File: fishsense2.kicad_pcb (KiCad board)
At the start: 2 copper layers, 86.4 x 49.5 mm, 39 parts, among them J1 Conn_02x10_Odd_Even, J11 Screw_Terminal_01x02, J2 BATT_OUT, J3 BATT_IN, K1 UMS05-1A80-75L, Q1 Q_NMOS_GSD, Q2 Q_NMOS_GSD, Q3 Q_NMOS_GSD, SW1 SW_Reed, SW2 SW_Reed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

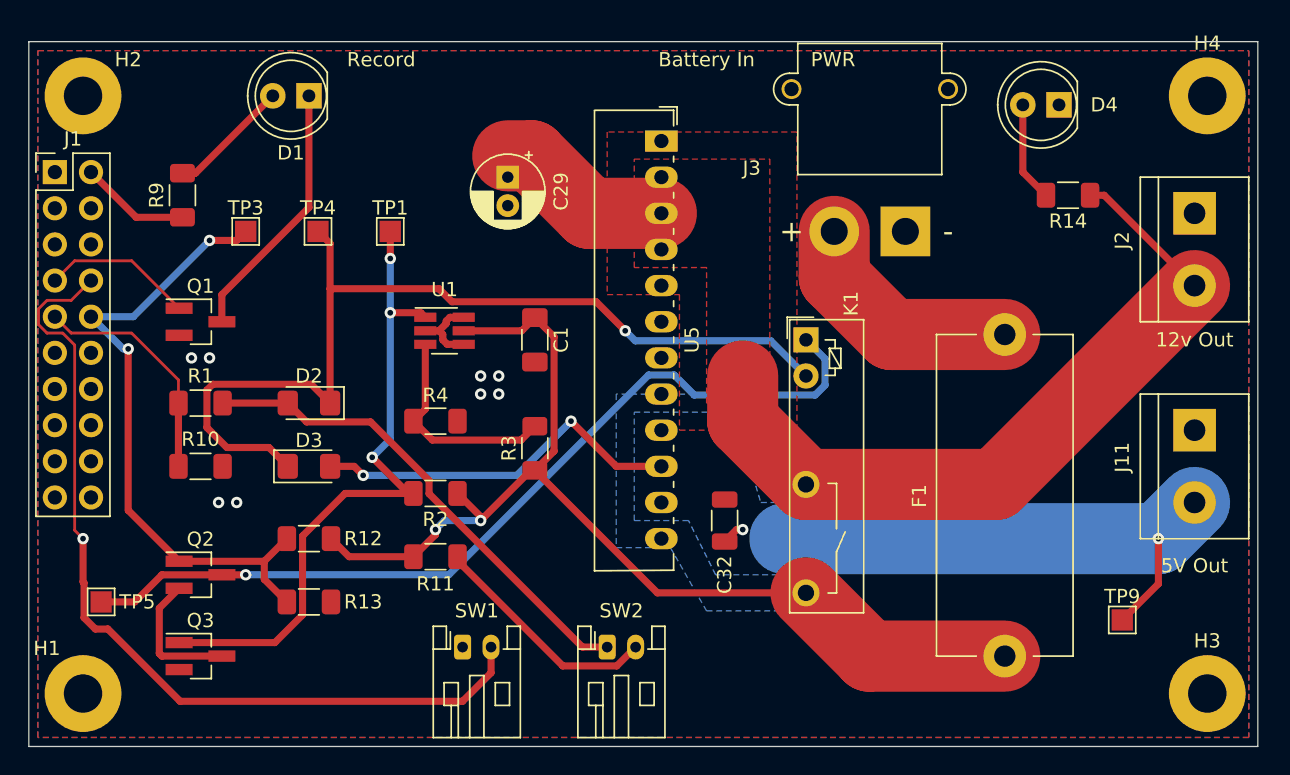
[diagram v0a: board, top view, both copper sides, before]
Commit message: Revised for BlueRobotics switch.
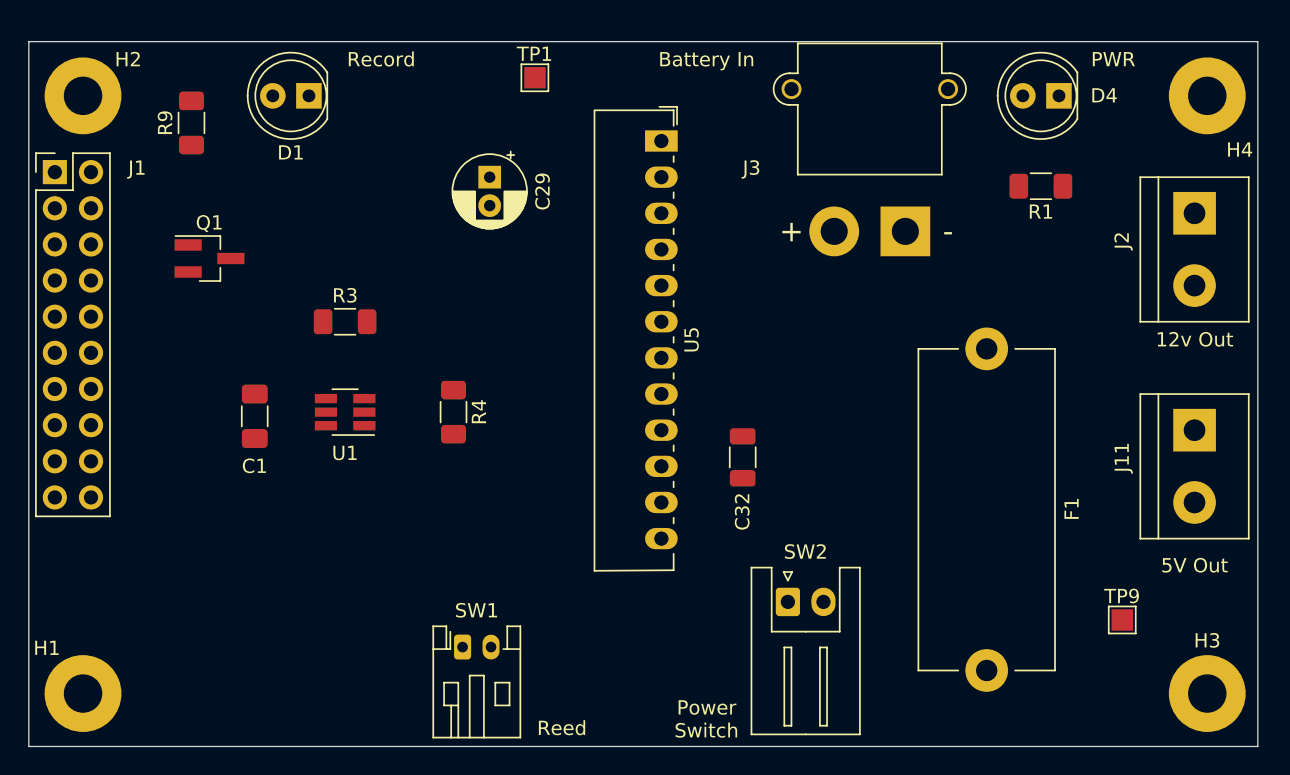
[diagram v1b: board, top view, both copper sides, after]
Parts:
- removed D2, D3: D, Diode_SMD:D_1206_3216Metric_Pad1.42x1.75mm_HandSolder
- removed K1: UMS05-1A80-75L, Relay_THT:Relay_SPST_TE_PCN-1xxD3MHZ
- removed Q2, Q3: Q_NMOS_GSD, Package_TO_SOT_SMD:SOT-23_Handsoldering
- removed R10: 10k, Resistor_SMD:R_1206_3216Metric_Pad1.30x1.75mm_HandSolder
- removed R11: 300, Resistor_SMD:R_1206_3216Metric_Pad1.30x1.75mm_HandSolder
- removed R12, R2: 100k, Resistor_SMD:R_1206_3216Metric_Pad1.30x1.75mm_HandSolder
- removed R13: 200k, Resistor_SMD:R_1206_3216Metric_Pad1.30x1.75mm_HandSolder
- removed R14: 1k, Resistor_SMD:R_1206_3216Metric_Pad1.30x1.75mm_HandSolder
- removed TP3: Relay_Ctl, TestPoint:TestPoint_Pad_1.5x1.5mm
- removed TP4: Relay+, TestPoint:TestPoint_Pad_1.5x1.5mm
- removed TP5: Relay-, TestPoint:TestPoint_Pad_1.5x1.5mm
- R1: value 30k -> 220
- R4: value 80k -> 71k5
- SW2: value SW_Reed -> SW_SPST; footprint Connector_JST:JST_PH_S2B-PH-K_1x02_P2.00mm_Horizontal -> Connector_JST:JST_XH_S2B-XH-A_1x02_P2.50mm_Horizontal
- TP1: value Poweroff_OD -> Poweroff
- moved R1 61.0 mm to (188.0, 121.9)
- moved F1 21.6 mm to (184.2, 133.3), turned to 270 degrees
- moved C1 20.4 mm to (132.7, 138.1)
- moved R3 16.0 mm to (139.1, 131.4), turned to 0 degrees
- moved TP1 14.8 mm to (152.4, 114.3)
- moved SW2 13.1 mm to (170.2, 151.1)
- moved U1 9.03 mm to (139.1, 137.8), turned to 180 degrees
- moved R9 5.12 mm to (128.3, 117.5)
- moved C32 4.62 mm to (167.0, 141.0)
- moved Q1 4.49 mm to (129.5, 127.0)
- moved R4 1.42 mm to (146.7, 137.8), turned to 270 degrees
- moved C29 1.27 mm to (149.2, 121.3)
- moved D4 0.64 mm to (189.2, 115.6)
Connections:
- C29 pad 1: /Power/BATT_SWITCHED -> +12V
- J2 pad 2: /Power/BATT_SWITCHED -> +12V
- J3 pad 2: Net-(F1-Pad2) -> Net-(J3-Pad2)
- R1 pad 1: Net-(D2-Pad2) -> +5V
- R1 pad 2: REED -> Net-(D4-Pad2)
- SW2 pad 1: Net-(D2-Pad2) -> Net-(J3-Pad2)
- SW2 pad 2: Net-(R11-Pad2) -> Net-(F1-Pad2)
- U5 pad 1: Net-(U5-Pad1) -> /Power/POWEROFF_OD
- U5 pad 2: /Power/BATT_SWITCHED -> +12V
- U5 pad 3: /Power/BATT_SWITCHED -> +12V
- U5 pad 4: /Power/BATT_SWITCHED -> +12V
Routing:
- net +12V: track 75.8 -> 0.00 mm, vias 2 -> 0
- net /Power/RELAY+: track 67.2 -> 0.00 mm, vias 1 -> 0
- net /Power/BATT_SWITCHED: track 65.0 -> 0.00 mm
- net +5V: track 64.7 -> 0.00 mm, vias 4 -> 0
- net /Power/RELAY-: track 62.1 -> 0.00 mm, vias 1 -> 0
- net Net-(J1-Pad8): track 61.9 -> 0.00 mm, vias 1 -> 0
- net /Power/POWEROFF_OD: track 47.0 -> 0.00 mm, vias 3 -> 0
- net RELAY_CTL: track 45.1 -> 0.00 mm, vias 2 -> 0
- net Net-(D2-Pad2): track 34.7 -> 0.00 mm
- net Net-(D1-Pad1): track 18.4 -> 0.00 mm
- net Net-(F1-Pad2): track 16.9 -> 0.00 mm
- net REED: track 16.6 -> 0.00 mm
- net Net-(R11-Pad2): track 16.4 -> 0.00 mm
- net Net-(R3-Pad2): track 15.2 -> 0.00 mm
- net Net-(J1-Pad7): track 10.7 -> 0.00 mm
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- removed copper zone on B.Cu, net +5V
- removed copper zone on F.Cu, net /Power/BATT_SWITCHED
- removed copper zone on B.Cu, net GND
- removed copper zone on F.Cu, net GND
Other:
- board text added: "Power Switch"
- board text added: "Reed"

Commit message: Routed Traces
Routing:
- net +5V: track 0.00 -> 90.2 mm, vias 0 -> 1
- net +12V: track 0.00 -> 88.1 mm
- net (no net): track 0.00 -> 46.1 mm
- net /Power/POWEROFF_OD: track 0.00 -> 42.2 mm
- net Net-(J1-Pad8): track 0.00 -> 40.8 mm
- net Net-(J3-Pad2): track 0.00 -> 28.1 mm
- net GND: track 0.00 -> 21.7 mm, vias 0 -> 1
- net Net-(D1-Pad1): track 0.00 -> 13.7 mm
- net Net-(F1-Pad2): track 0.00 -> 12.2 mm
- net Net-(R3-Pad2): track 0.00 -> 12.0 mm
- net Net-(J1-Pad7): track 0.00 -> 10.4 mm
- net Net-(J1-Pad2): track 0.00 -> 7.85 mm
- net Net-(D4-Pad2): track 0.00 -> 6.47 mm
- net Net-(D1-Pad2): track 0.00 -> 6.36 mm
- added copper zone on B.Cu, net GND
- added copper zone on F.Cu, net GND
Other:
- net class Power added: clearance 0.4, trace_width 5, via_dia 0.8, via_drill 0.4

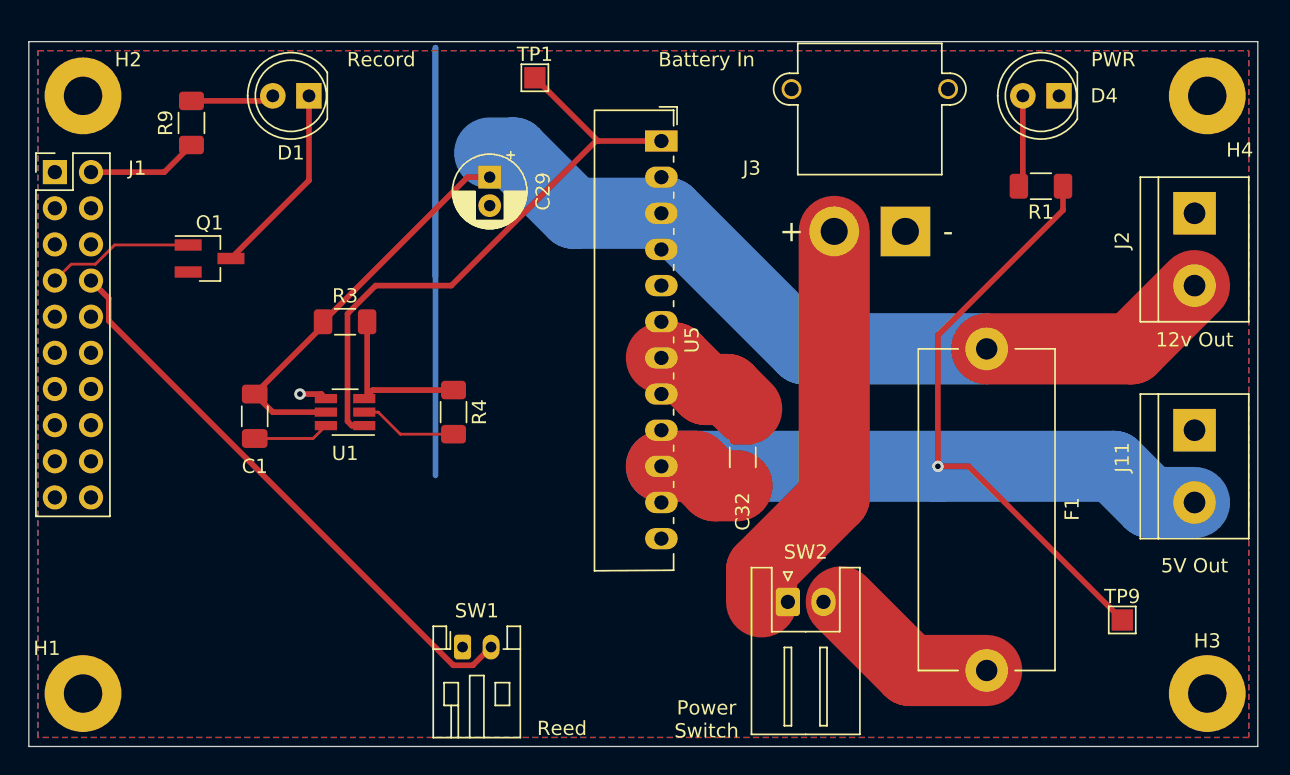
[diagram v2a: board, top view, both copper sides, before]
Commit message: Added load switch
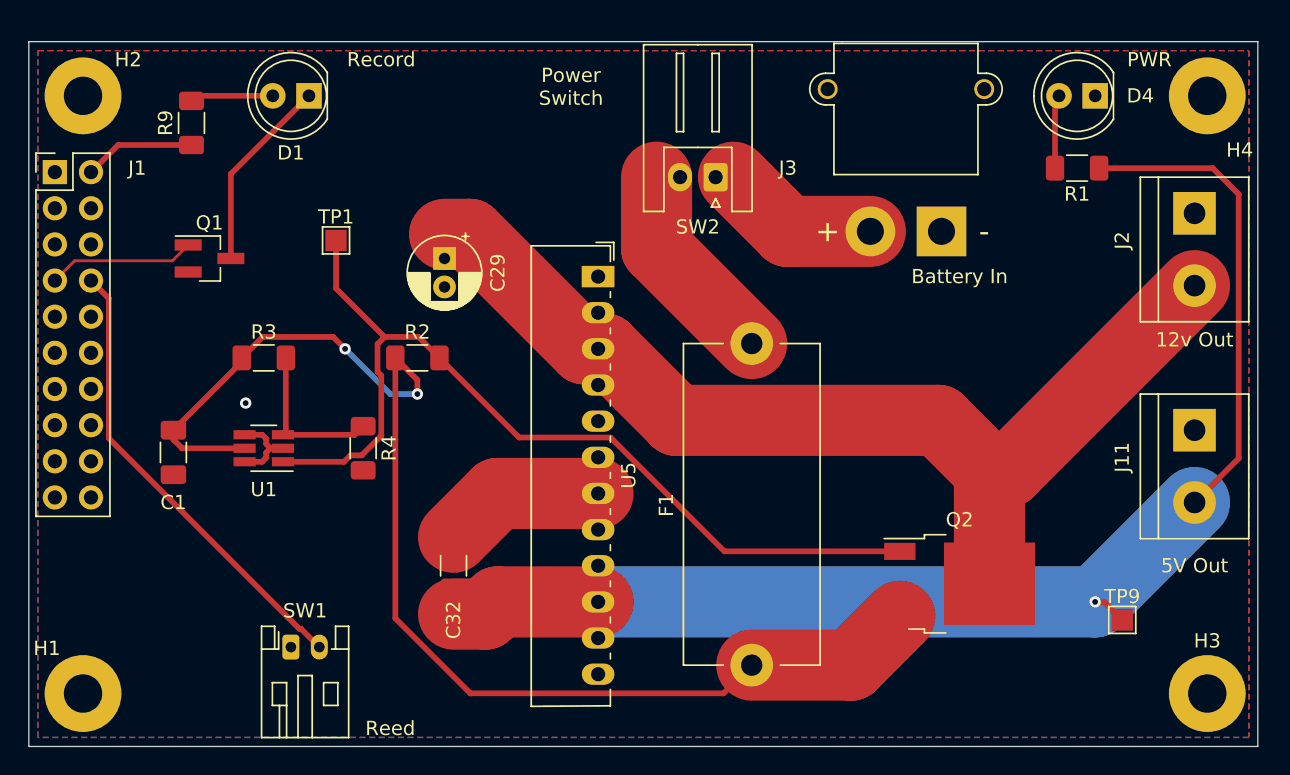
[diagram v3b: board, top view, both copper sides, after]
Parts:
- added Q2: Q_PMOS_GDS, Package_TO_SOT_SMD:TO-252-2, F.Cu at (182.2, 149.9)
- added R2: 100k, Resistor_SMD:R_1206_3216Metric_Pad1.30x1.75mm_HandSolder, F.Cu at (144.1, 134.0)
- moved SW2 30.3 mm to (165.1, 121.3), turned to 180 degrees
- moved F1 27.7 mm to (167.6, 155.6), turned to 90 degrees
- moved C32 21.7 mm to (146.7, 148.6)
- moved TP1 18.1 mm to (138.4, 125.7)
- moved SW1 12.1 mm to (135.3, 154.3)
- moved U5 10.5 mm to (156.8, 128.3)
- moved R4 6.84 mm to (140.3, 140.3)
- moved C29 6.54 mm to (146.1, 127.0)
- moved R3 6.25 mm to (133.3, 134.0)
- moved U1 6.25 mm to (133.3, 140.3)
- moved C1 6.25 mm to (127.0, 140.6)
- moved R1 2.84 mm to (190.5, 120.7)
- moved D4 2.54 mm to (191.8, 115.6)
- moved J3 2.54 mm to (181.0, 125.1)
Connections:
- C29 pad 1: +12V -> /Power/BATT_SWITCHED
- J2 pad 2: +12V -> /Power/BATT_SWITCHED
- U5 pad 1: /Power/POWEROFF_OD -> Net-(U5-Pad1)
- U5 pad 2: +12V -> /Power/BATT_SWITCHED
- U5 pad 3: +12V -> /Power/BATT_SWITCHED
- U5 pad 4: +12V -> /Power/BATT_SWITCHED
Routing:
- net /Power/BATT_SWITCHED: track 0.00 -> 72.9 mm
- net (no net): track 46.1 -> 0.00 mm
- net /Power/POWEROFF_OD: track 42.2 -> 65.6 mm
- net Net-(J3-Pad2): track 28.1 -> 11.2 mm
- net Net-(J1-Pad8): track 40.8 -> 32.5 mm
- net GND: track 21.7 -> 17.2 mm
- net Net-(F1-Pad2): track 12.2 -> 14.5 mm
- net +5V: track 90.2 -> 91.7 mm
- net Net-(D4-Pad2): track 6.47 -> 5.20 mm
- net +12V: track 88.1 -> 89.0 mm, vias 0 -> 2
- net Net-(R3-Pad2): track 12.0 -> 11.4 mm
- net Net-(D1-Pad2): track 6.36 -> 5.86 mm

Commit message: Some footprint and part changes based on availability.
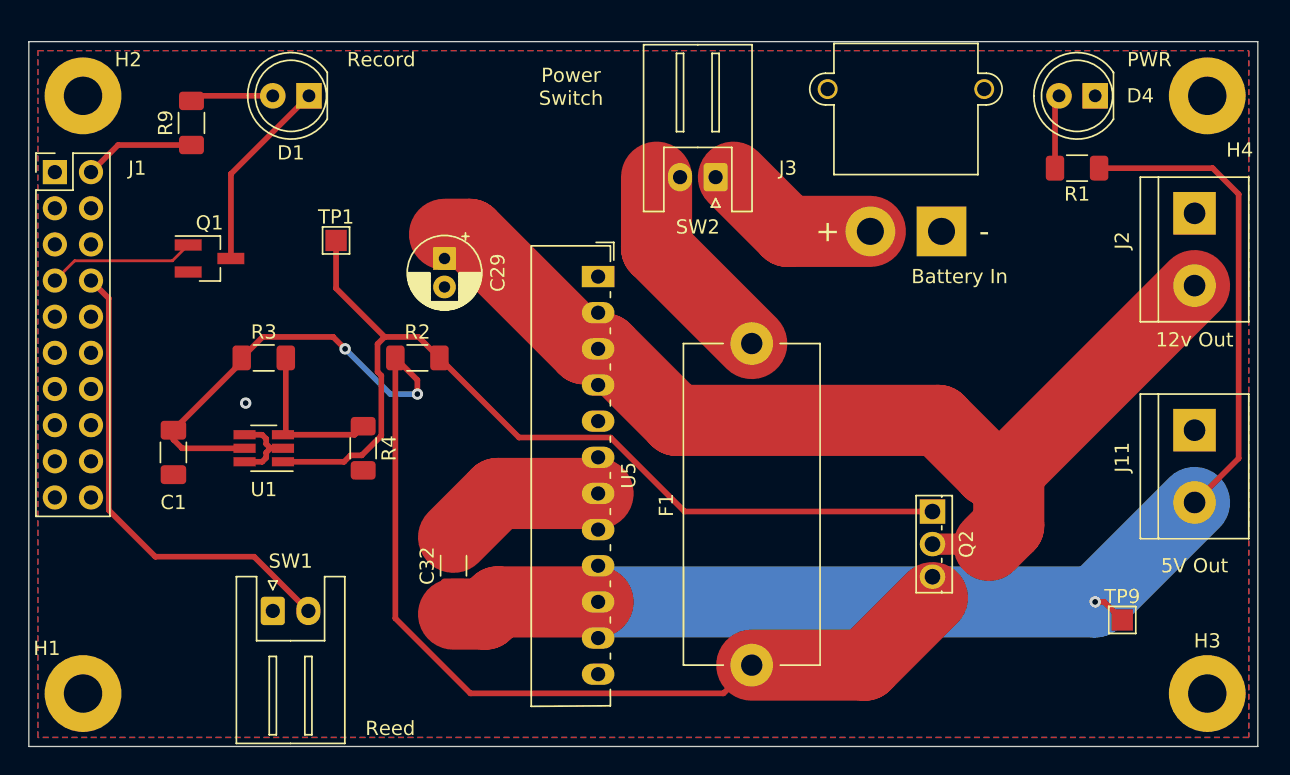
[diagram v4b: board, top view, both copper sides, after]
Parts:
- C32: footprint Capacitor_SMD:C_1206_3216Metric -> Capacitor_SMD:C_1206_3216Metric_Pad1.33x1.80mm_HandSolder
- Q2: footprint Package_TO_SOT_SMD:TO-252-2 -> Package_TO_SOT_THT:TO-251-3_Vertical
- SW1: footprint Connector_JST:JST_PH_S2B-PH-K_1x02_P2.00mm_Horizontal -> Connector_JST:JST_XH_S2B-XH-A_1x02_P2.50mm_Horizontal
- moved Q2 5.43 mm to (180.3, 144.8), turned to 270 degrees
- moved SW1 2.84 mm to (134.0, 151.8)
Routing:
- net /Power/BATT_SWITCHED: track 72.9 -> 78.0 mm
- net +12V: track 89.0 -> 91.8 mm
- net Net-(J1-Pad8): track 32.5 -> 33.6 mm
- net /Power/POWEROFF_OD: track 65.6 -> 66.7 mm

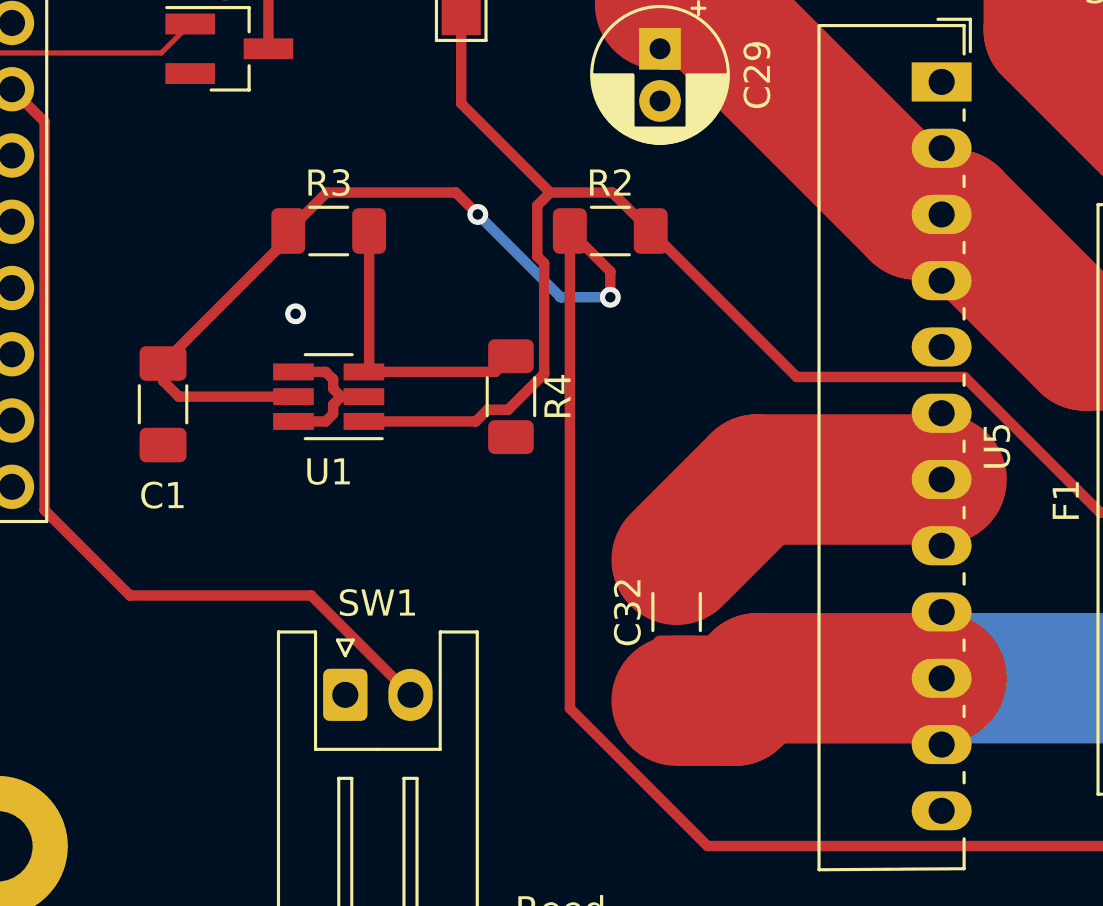
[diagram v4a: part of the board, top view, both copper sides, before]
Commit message: Replaced tps3711 with different part which is in stock.
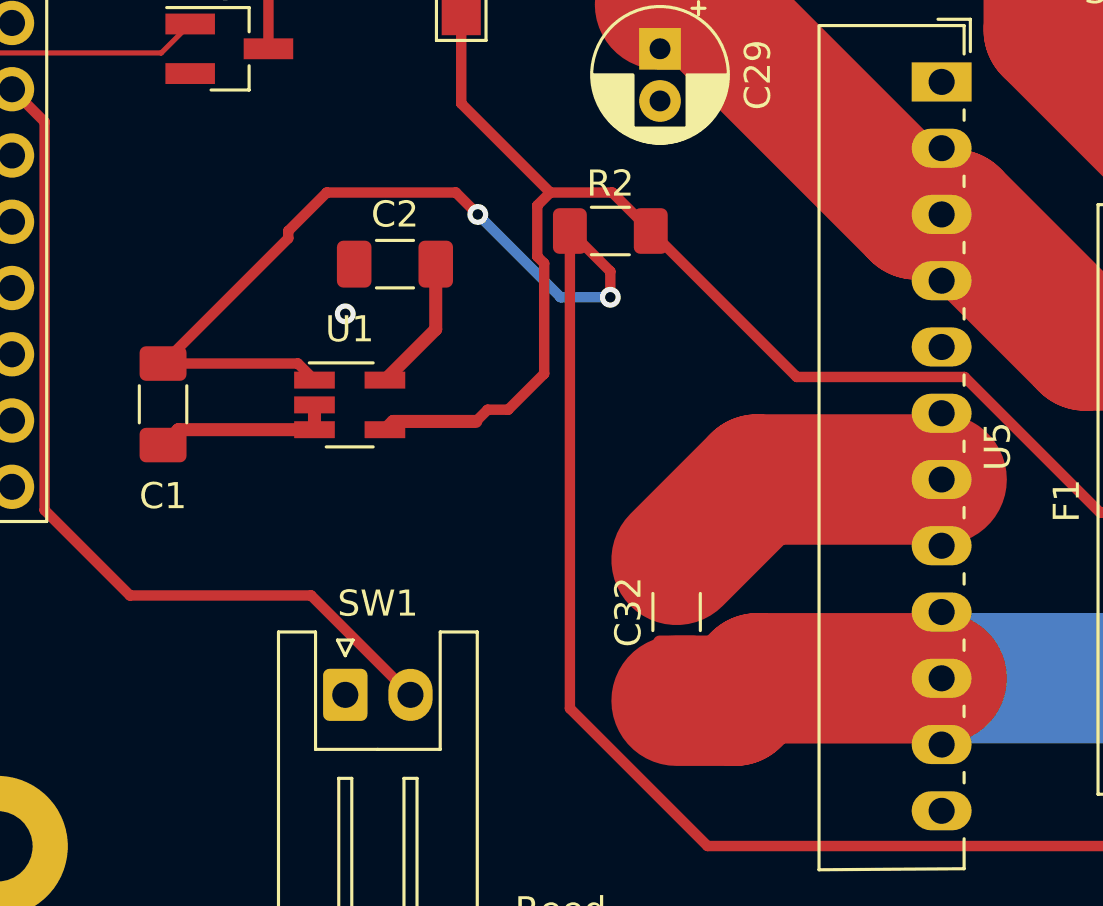
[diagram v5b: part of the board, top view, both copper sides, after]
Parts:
- removed R3: 1M69, Resistor_SMD:R_1206_3216Metric_Pad1.30x1.75mm_HandSolder
- removed R4: 71k5, Resistor_SMD:R_1206_3216Metric_Pad1.30x1.75mm_HandSolder
- added C2: 10n, Capacitor_SMD:C_1206_3216Metric_Pad1.33x1.80mm_HandSolder, F.Cu at (135.9, 135.3)
- U1: value TPS3711 -> R3119; footprint Package_TO_SOT_SMD:SOT-23-6_Handsoldering -> Package_TO_SOT_SMD:SOT-23-5_HandSoldering
- moved U1 0.86 mm to (134.2, 140.7), turned to 0 degrees
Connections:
- U1 pad 1: /Power/POWEROFF_OD -> +12V
- U1 pad 3: Net-(R3-Pad2) -> GND
- U1 pad 4: GND -> /Power/POWEROFF_OD
- U1 pad 5: +12V -> Net-(C2-Pad1)
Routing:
- net Net-(R3-Pad2): track 11.4 -> 0.00 mm
- net Net-(C2-Pad1): track 0.00 -> 5.25 mm
- net +5V: track 91.7 -> 96.7 mm
- net GND: track 17.2 -> 18.4 mm
- net /Power/POWEROFF_OD: track 66.7 -> 66.0 mm
